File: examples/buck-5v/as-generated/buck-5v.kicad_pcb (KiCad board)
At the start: 2 copper layers, 126 x 56 mm, 11 parts, among them J1 12V IN, J2 5V OUT, U1 LM2596S-5

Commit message: Regenerate the five with stitched pours, silk that speaks, and wires that never double back
All ten variants rebuilt by the fixed generator: reviewed boards carry
ground on both faces with the stitching ring (buck 35 vias, fpga 116),
thru_hole_only front pours, the board id and connector pin names in
silk, and the buck's explicit ground return; the sheets hook power up
through upright symbols and source-anchored flags with no overlapping
wires and no junction-less tees left. Every reviewed variant passes its
own gate with zero errors; every as-generated variant still fails, now
also for the rules this round added.

Co-Authored-By: Claude Fable 5 <noreply@anthropic.com>
Claude-Session: https://claude.ai/code/session_01DUj7Ltu92tWg159mCSacwY
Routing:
- net GND: track 111.8 -> 205.8 mm
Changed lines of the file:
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@@
 	(segment (start 221.23 95.83) (end 221.0 110.0) (width 0.25) (layer "F.Cu") (net 1))
 	(segment (start 221.0 110.0) (end 210.0 110.0) (width 0.25) (layer "F.Cu") (net 1))
+	(segment (start 116.0 110.0) (end 210.0 110.0) (width 0.25) (layer "F.Cu") (net 1))
 	(segment (start 154.58 71.83) (end 151.0 72.0) (width 0.25) (layer "F.Cu") (net 1))
 	(segment (start 154.58 75.23) (end 154.35 80.0) (width 0.25) (layer "F.Cu") (net 1))

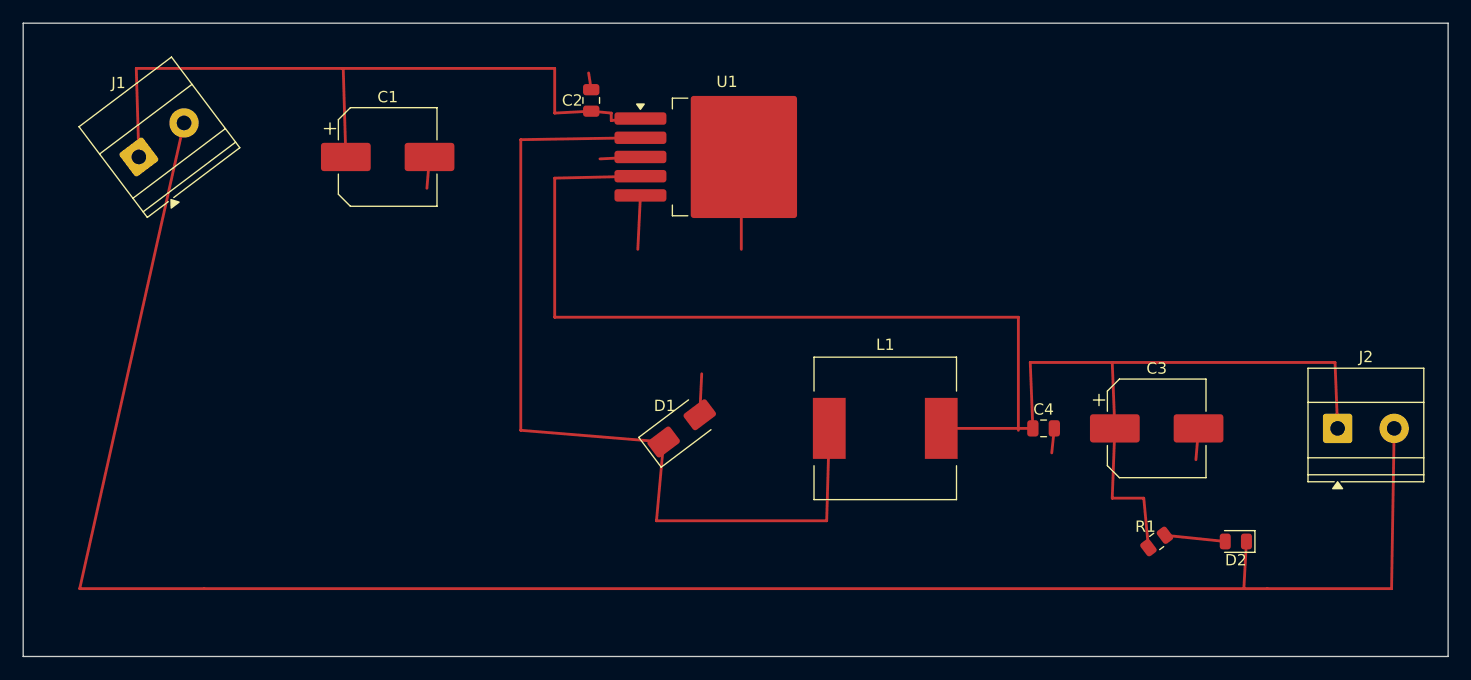
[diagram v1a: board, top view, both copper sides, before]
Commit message: Regenerate the five as round three drew them
All five reviewed projects pass their gates again: the buck all wire
with its feedback drawn home, the motor's logic named at the header,
the carrier reading as the pinout table it is - with its feed diode
finally pointing the right way - the filter compact with test points,
and the FPGA's capacitors sitting beside the units they feed. Thirty
renders redrawn, verdict tables at today's numbers.

Co-Authored-By: Claude Fable 5 <noreply@anthropic.com>
Claude-Session: https://claude.ai/code/session_01DUj7Ltu92tWg159mCSacwY
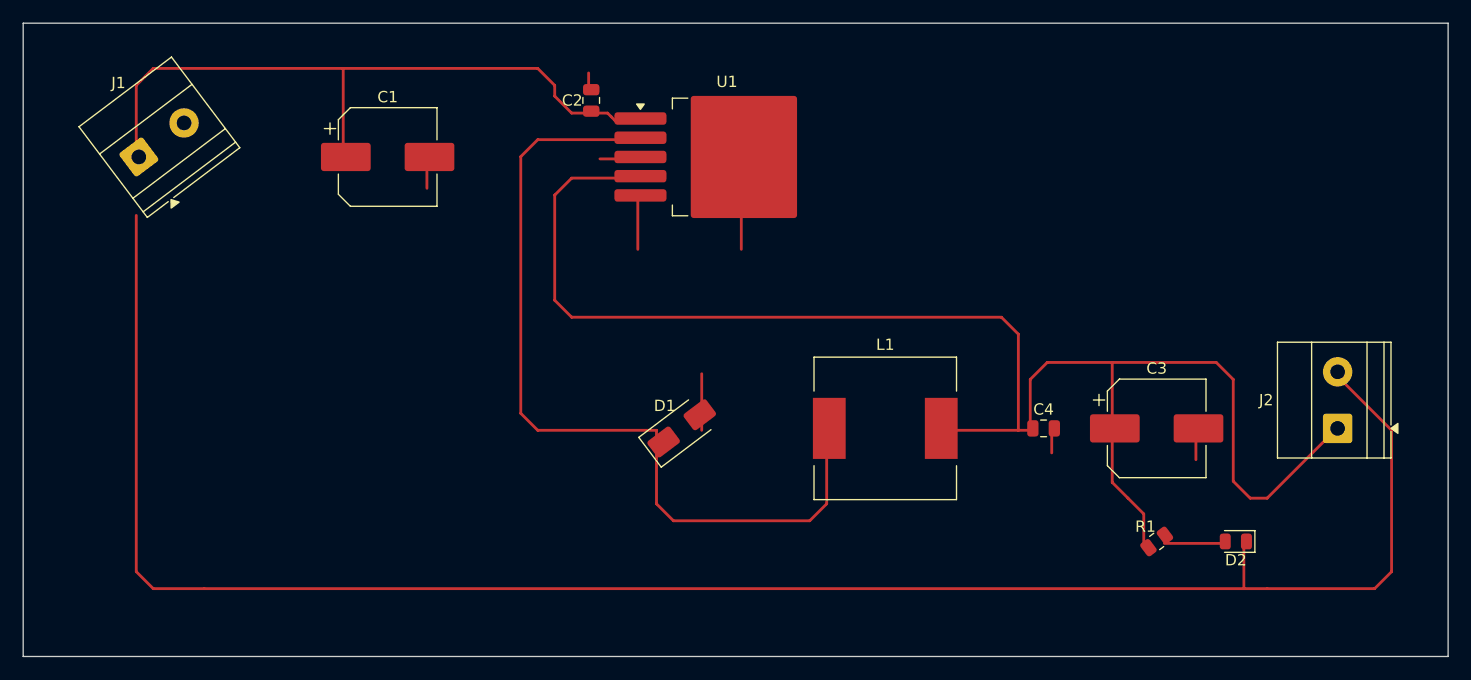
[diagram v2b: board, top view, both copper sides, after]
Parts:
- turned J2 to 90 degrees
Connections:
- net +12V renamed /+12V
- net +5V renamed /+5V
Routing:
- net GND: track 205.8 -> 197.1 mm
- net /SW: track 79.2 -> 75.6 mm
- net /+12V: track 64.9 -> 61.9 mm
- net /+5V: track 136.8 -> 138.1 mm

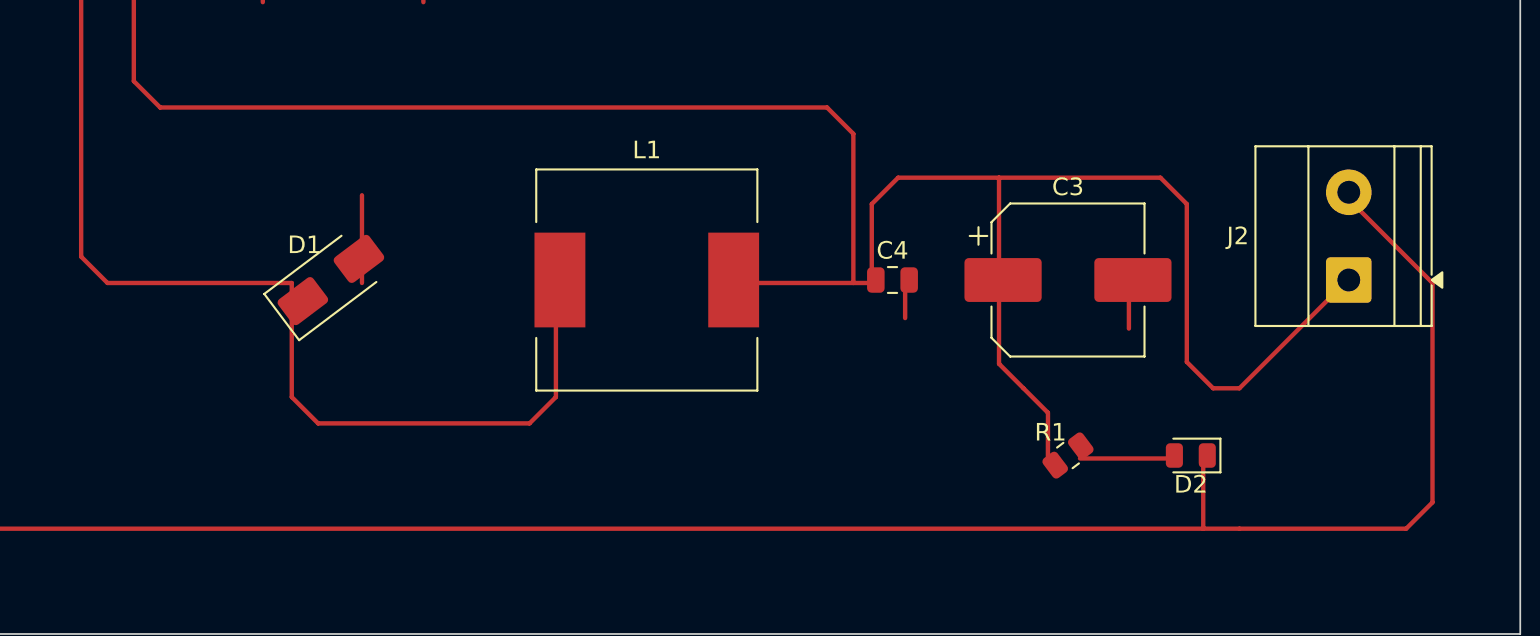
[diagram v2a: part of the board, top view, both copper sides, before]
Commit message: Regenerate the four the text and width work changed
Designators and values off the rails they were printed on, power-named
nets at the width their rule asks for, and the buck's feedback ending
on the capacitor pad it senses at.

Co-Authored-By: Claude Fable 5 <noreply@anthropic.com>
Claude-Session: https://claude.ai/code/session_01DUj7Ltu92tWg159mCSacwY
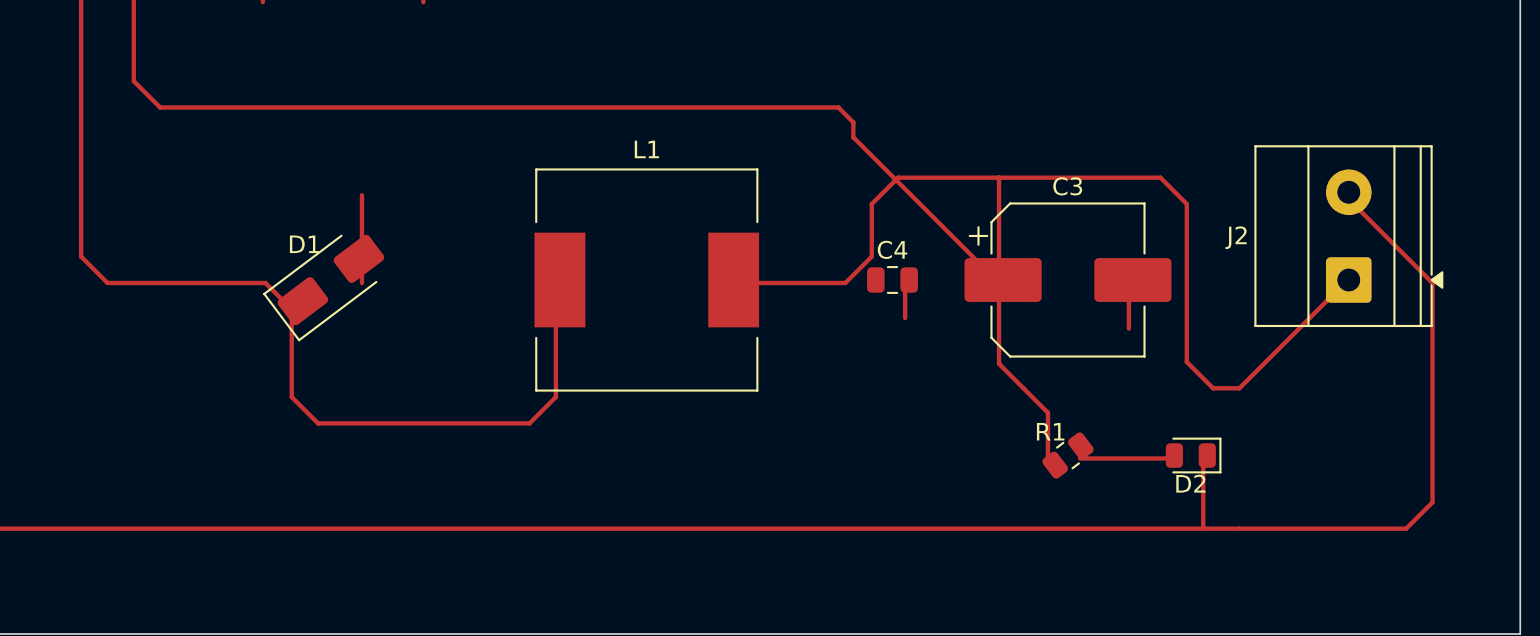
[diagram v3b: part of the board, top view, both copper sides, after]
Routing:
- net /+5V: track 138.1 -> 141.0 mm
- net /SW: track 75.6 -> 74.7 mm
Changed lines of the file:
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@@
 	(segment (start 144.0 71.8) (end 144.0 94.5) (width 0.25) (layer "F.Cu") (net 5))
 	(segment (start 144.0 94.5) (end 145.5 96.0) (width 0.25) (layer "F.Cu") (net 5))
-	(segment (start 145.5 96.0) (end 156.0 96.0) (width 0.25) (layer "F.Cu") (net 5))
-	(segment (start 156.0 96.0) (end 156.0 102.5) (width 0.25) (layer "F.Cu") (net 5))
+	(segment (start 145.5 96.0) (end 154.5 96.0) (width 0.25) (layer "F.Cu") (net 5))
+	(segment (start 154.5 96.0) (end 156.0 97.5) (width 0.25) (layer "F.Cu") (net 5))
+	(segment (start 156.0 97.5) (end 156.0 102.5) (width 0.25) (layer "F.Cu") (net 5))
 	(segment (start 156.0 102.5) (end 157.5 104.0) (width 0.25) (layer "F.Cu") (net 5))
 	(segment (start 157.5 104.0) (end 169.55 104.0) (width 0.25) (layer "F.Cu") (net 5))
@@
 	(segment (start 147.0 75.2) (end 147.0 84.5) (width 0.25) (layer "F.Cu") (net 3))
 	(segment (start 147.0 84.5) (end 148.5 86.0) (width 0.25) (layer "F.Cu") (net 3))
-	(segment (start 148.5 86.0) (end 186.5 86.0) (width 0.25) (layer "F.Cu") (net 3))
-	(segment (start 186.5 86.0) (end 188.0 87.5) (width 0.25) (layer "F.Cu") (net 3))
-	(segment (start 188.0 87.5) (end 188.0 96.0) (width 0.25) (layer "F.Cu") (net 3))
-	(segment (start 180.95 96.0) (end 189.05 96.0) (width 0.25) (layer "F.Cu") (net 3))
-	(segment (start 189.05 96.0) (end 189.05 91.5) (width 0.25) (layer "F.Cu") (net 3))
+	(segment (start 148.5 86.0) (end 187.15 86.0) (width 0.25) (layer "F.Cu") (net 3))
+	(segment (start 187.15 86.0) (end 188.0 86.85) (width 0.25) (layer "F.Cu") (net 3))
+	(segment (start 188.0 86.85) (end 188.0 87.7) (width 0.25) (layer "F.Cu") (net 3))
+	(segment (start 188.0 87.7) (end 196.3 96.0) (width 0.25) (layer "F.Cu") (net 3))
+	(segment (start 180.95 96.0) (end 187.55 96.0) (width 0.25) (layer "F.Cu") (net 3))
+	(segment (start 187.55 96.0) (end 189.05 94.5) (width 0.25) (layer "F.Cu") (net 3))
+	(segment (start 189.05 94.5) (end 189.05 91.5) (width 0.25) (layer "F.Cu") (net 3))
 	(segment (start 189.05 91.5) (end 190.55 90.0) (width 0.25) (layer "F.Cu") (net 3))
 	(segment (start 190.55 90.0) (end 196.3 90.0) (width 0.25) (layer "F.Cu") (net 3))
@@
 	(segment (start 110.0 108.5) (end 111.5 110.0) (width 0.25) (layer "F.Cu") (net 1))
 	(segment (start 111.5 110.0) (end 116.0 110.0) (width 0.25) (layer "F.Cu") (net 1))
-	(segment (start 216.0 91.0) (end 221.0 96.0) (width 0.25) (layer "F.Cu") (net 1))
-	(segment (start 221.0 96.0) (end 221.0 108.5) (width 0.25) (layer "F.Cu") (net 1))
-	(segment (start 221.0 108.5) (end 219.5 110.0) (width 0.25) (layer "F.Cu") (net 1))
-	(segment (start 219.5 110.0) (end 210.0 110.0) (width 0.25) (layer "F.Cu") (net 1))
 	(segment (start 116.0 110.0) (end 210.0 110.0) (width 0.25) (layer "F.Cu") (net 1))
+	(segment (start 210.0 110.0) (end 219.5 110.0) (width 0.25) (layer "F.Cu") (net 1))
+	(segment (start 219.5 110.0) (end 221.0 108.5) (width 0.25) (layer "F.Cu") (net 1))
+	(segment (start 221.0 108.5) (end 221.0 96.0) (width 0.25) (layer "F.Cu") (net 1))
+	(segment (start 221.0 96.0) (end 216.0 91.0) (width 0.25) (layer "F.Cu") (net 1))
 	(segment (start 154.35 72.0) (end 151.0 72.0) (width 0.25) (layer "F.Cu") (net 1))
 	(segment (start 154.35 75.4) (end 154.35 80.0) (width 0.25) (layer "F.Cu") (net 1))
